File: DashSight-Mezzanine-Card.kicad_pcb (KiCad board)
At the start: 4 copper layers, 72 x 78.5 mm, 95 parts, among them IC2 ELM327, J1 Pi2 Connector, J10 QWIIC_CONNECTORJS-1MM, J14 1W-PC16, J15 1W-PC9, J2 Euler Connector, J3 Conn_Coaxial, J4 OBD2-DB9_Male, J5 Conn_02x05_Odd_Even, J6 Safeboot, J7 Reset, J8 QWIIC_CONNECTORJS-1MM, J9 QWIIC_CONNECTORJS-1MM, Q1 2N3904, Q2 2N3906, Q3 2N3906, Q4 2N3904, Q5 2N3904, Q6 2N3904, Q7 2N3904, SW1 SW_Push, SW2 SW_Push, U1 MCP2561-E/P, U2 LM317L_TO92, U3 LP2950-3.0_TO92, U4 ADuM1201AR, U5 NEO-M9N, U6 LSM9DS1, Y1 4.0MHz

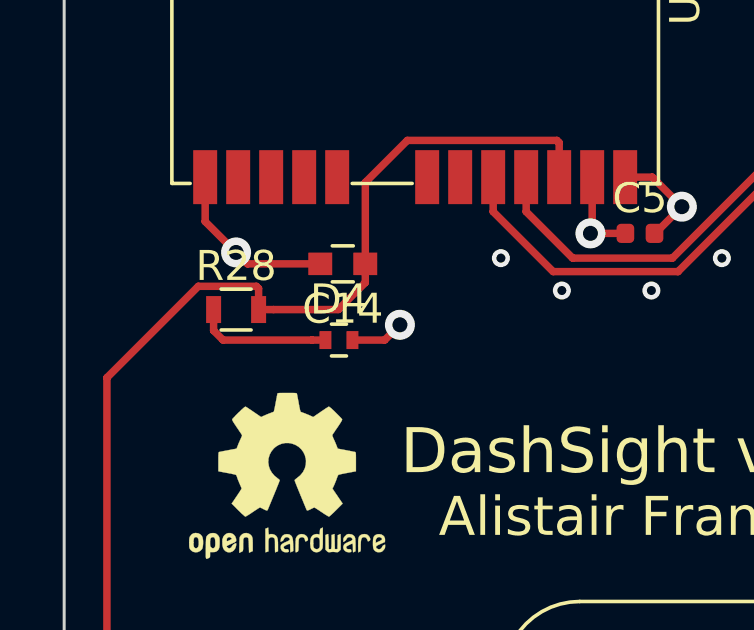
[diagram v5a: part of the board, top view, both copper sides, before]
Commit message: Update based on BOM avaliability
Signed-off-by: Alistair Francis <alistair@alistair23.me>
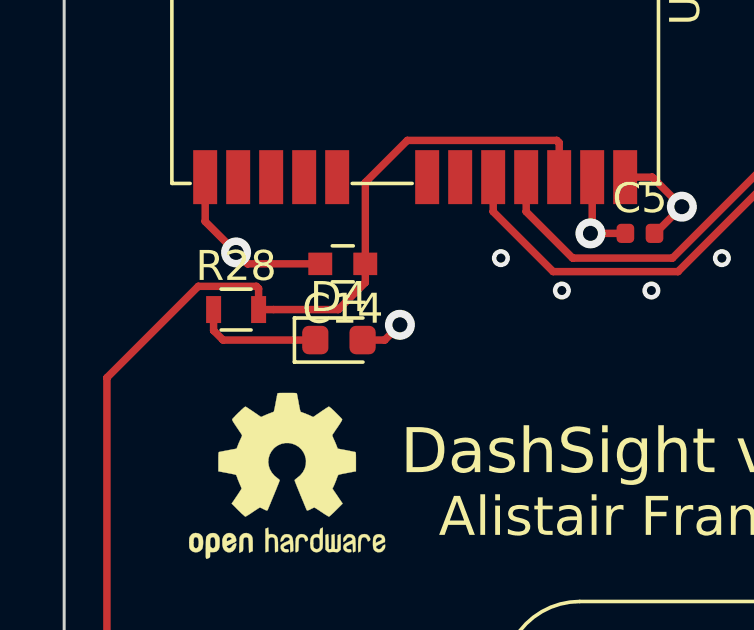
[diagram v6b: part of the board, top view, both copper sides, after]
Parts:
- D4: footprint Resistors_SMD:R_0402 -> Diode_SMD:D_0603_1608Metric
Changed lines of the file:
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@@
     (thickness 1.6)
     (drawings 6)
-    (tracks 916)
+    (tracks 915)
     (zones 0)
     (modules 95)
@@
     (uvia_drill 0.1)
   )
+  (module Diode_SMD:D_0603_1608Metric (layer F.Cu)
+    (at 137.16 76.2)
+    (descr "Diode SMD 0603 (1608 Metric), square (rectangular) end terminal, IPC_7351 nominal, (Body size source: http://www.tortai-tech.com/upload/download/2011102023233369053.pdf), generated with kicad-footprint-generator")
+    (tags diode)
+    (attr smd)
+    (fp_text reference D4 (at 0 -1.43) (layer F.SilkS)
+      (effects (font (size 1 1) (thickness 0.15)))
+    )
+    (fp_text value 0.5A/40V/420mV (at 0 1.43) (layer F.Fab)
+      (effects (font (size 1 1) (thickness 0.15)))
+    )
+    (fp_text user %R (at 0 0) (layer F.Fab)
+      (effects (font (size 0.4 0.4) (thickness 0.06)))
+    )
+    (fp_line (start 1.48 0.73) (end -1.48 0.73) (layer F.CrtYd) (width 0.05))
+    (fp_line (start 1.48 -0.73) (end 1.48 0.73) (layer F.CrtYd) (width 0.05))
+    (fp_line (start -1.48 -0.73) (end 1.48 -0.73) (layer F.CrtYd) (width 0.05))
+    (fp_line (start -1.48 0.73) (end -1.48 -0.73) (layer F.CrtYd) (width 0.05))
+    (fp_line (start -1.485 0.735) (end 0.8 0.735) (layer F.SilkS) (width 0.12))
+    (fp_line (start -1.485 -0.735) (end -1.485 0.735) (layer F.SilkS) (width 0.12))
+    (fp_line (start 0.8 -0.735) (end -1.485 -0.735) (layer F.SilkS) (width 0.12))
+    (fp_line (start 0.8 0.4) (end 0.8 -0.4) (layer F.Fab) (width 0.1))
+    (fp_line (start -0.8 0.4) (end 0.8 0.4) (layer F.Fab) (width 0.1))
+    (fp_line (start -0.8 -0.1) (end -0.8 0.4) (layer F.Fab) (width 0.1))
+    (fp_line (start -0.5 -0.4) (end -0.8 -0.1) (layer F.Fab) (width 0.1))
+    (fp_line (start 0.8 -0.4) (end -0.5 -0.4) (layer F.Fab) (width 0.1))
+    (pad 2 smd roundrect (at 0.7875 0) (size 0.875 0.95) (layers F.Cu F.Paste F.Mask) (roundrect_rratio 0.25)
+      (net 35 +3V3))
+    (pad 1 smd roundrect (at -0.7875 0) (size 0.875 0.95) (layers F.Cu F.Paste F.Mask) (roundrect_rratio 0.25)
+      (net 51 "Net-(D4-Pad1)"))
+    (model ${KISYS3DMOD}/Diode_SMD.3dshapes/D_0603_1608Metric.wrl
+      (at (xyz 0 0 0))
+      (scale (xyz 1 1 1))
+      (rotate (xyz 0 0 0))
+    )
+  )
   (module Crystal:Crystal_HC49-U_Vertical (layer F.Cu)
     (at 150.749 87.4395 180)
@@
     )
   )
-  (module Resistors_SMD:R_0402 (layer F.Cu)
-    (at 137.16 76.2)
-    (descr "Resistor SMD 0402, reflow soldering, Vishay (see dcrcw.pdf)")
-    (tags "resistor 0402")
-    (attr smd)
-    (fp_text reference D4 (at 0 -1.35) (layer F.SilkS)
-      (effects (font (size 1 1) (thickness 0.15)))
-    )
-    (fp_text value 0.5A/40V/420mV (at 0 1.45) (layer F.Fab)
-      (effects (font (size 1 1) (thickness 0.15)))
-    )
-    (fp_text user %R (at 0 -1.35) (layer F.Fab)
-      (effects (font (size 1 1) (thickness 0.15)))
-    )
-    (fp_line (start -0.5 0.25) (end -0.5 -0.25) (layer F.Fab) (width 0.1))
-    (fp_line (start 0.5 0.25) (end -0.5 0.25) (layer F.Fab) (width 0.1))
-    (fp_line (start 0.5 -0.25) (end 0.5 0.25) (layer F.Fab) (width 0.1))
-    (fp_line (start -0.5 -0.25) (end 0.5 -0.25) (layer F.Fab) (width 0.1))
-    (fp_line (start 0.25 -0.53) (end -0.25 -0.53) (layer F.SilkS) (width 0.12))
-    (fp_line (start -0.25 0.53) (end 0.25 0.53) (layer F.SilkS) (width 0.12))
-    (fp_line (start -0.8 -0.45) (end 0.8 -0.45) (layer F.CrtYd) (width 0.05))
-    (fp_line (start -0.8 -0.45) (end -0.8 0.45) (layer F.CrtYd) (width 0.05))
-    (fp_line (start 0.8 0.45) (end 0.8 -0.45) (layer F.CrtYd) (width 0.05))
-    (fp_line (start 0.8 0.45) (end -0.8 0.45) (layer F.CrtYd) (width 0.05))
-    (pad 1 smd rect (at -0.45 0) (size 0.4 0.6) (layers F.Cu F.Paste F.Mask)
-      (net 51 "Net-(D4-Pad1)"))
-    (pad 2 smd rect (at 0.45 0) (size 0.4 0.6) (layers F.Cu F.Paste F.Mask)
-      (net 35 +3V3))
-    (model ${KISYS3DMOD}/Resistors_SMD.3dshapes/R_0402.wrl
-      (at (xyz 0 0 0))
-      (scale (xyz 1 1 1))
-      (rotate (xyz 0 0 0))
-    )
-  )
   (module Diodes_SMD:D_SOD-123 (layer B.Cu)
     (at 146.939 115.824 180)
@@
   (gr_line (start 200 46.5) (end 200 125) (layer Edge.Cuts) (width 0.1))
   (gr_line (start 128 46.5) (end 200 46.5) (layer Edge.Cuts) (width 0.1))
+  (via (at 149.3139 53.2765) (size 0.6) (drill 0.3) (layers F.Cu B.Cu) (net 0))
   (via (at 138.4808 55.4228) (size 0.6) (drill 0.3) (layers F.Cu B.Cu) (net 1))
   (via (at 193.0908 59.7408) (size 0.8) (drill 0.4) (layers F.Cu B.Cu) (net 1))
@@
   (via (at 149.7203 58.0136) (size 0.6) (drill 0.3) (layers F.Cu B.Cu) (net 1))
   (via (at 149.7711 59.7789) (size 0.6) (drill 0.3) (layers F.Cu B.Cu) (net 1))
-  (via (at 149.3139 53.2765) (size 0.6) (drill 0.3) (layers F.Cu B.Cu) (net 0))
   (via (at 149.3139 54.4957) (size 0.6) (drill 0.3) (layers F.Cu B.Cu) (net 1))
   (via (at 151.0919 53.1241) (size 0.6) (drill 0.3) (layers F.Cu B.Cu) (net 1))
@@
   (segment (start 145.542 72.644) (end 146.708 72.644) (width 0.25) (layer F.Cu) (net 35))
   (segment (start 138.684 76.2) (end 139.192 75.692) (width 0.25) (layer F.Cu) (net 35))
-  (segment (start 137.61 76.2) (end 138.684 76.2) (width 0.25) (layer F.Cu) (net 35))
   (segment (start 187.706 121.963) (end 187.706 123.063) (width 0.25) (layer F.Cu) (net 35))
   (segment (start 187.781001 121.887999) (end 187.706 121.963) (width 0.25) (layer F.Cu) (net 35))
@@
   (segment (start 193.15684 74.76744) (end 192.9892 74.5998) (width 0.25) (layer F.Cu) (net 35))
   (segment (start 194.564 74.76744) (end 193.15684 74.76744) (width 0.25) (layer F.Cu) (net 35))
+  (segment (start 138.684 76.2) (end 137.9475 76.2) (width 0.25) (layer F.Cu) (net 35))
   (segment (start 141.0335 93.22963) (end 141.0335 94.361) (width 0.25) (layer F.Cu) (net 36))
   (segment (start 145.352999 86.364499) (end 141.0335 90.683998) (width 0.25) (layer F.Cu) (net 36))
@@
   (segment (start 164.792499 110.947501) (end 165.812501 110.947501) (width 0.25) (layer B.Cu) (net 50))
   (segment (start 157.7975 112.9665) (end 162.7735 112.9665) (width 0.25) (layer B.Cu) (net 50))
-  (segment (start 136.26 76.2) (end 136.71 76.2) (width 0.25) (layer F.Cu) (net 51))
-  (segment (start 133.297 76.2) (end 136.26 76.2) (width 0.25) (layer F.Cu) (net 51))
   (segment (start 132.981 75.884) (end 133.297 76.2) (width 0.25) (layer F.Cu) (net 51))
   (segment (start 132.981 75.184) (end 132.981 75.884) (width 0.25) (layer F.Cu) (net 51))
+  (segment (start 133.297 76.2) (end 136.3725 76.2) (width 0.25) (layer F.Cu) (net 51))
   (segment (start 140.3605 54.028) (end 140.081 54.3075) (width 0.25) (layer F.Cu) (net 52))
   (segment (start 140.3605 52.197) (end 140.3605 54.028) (width 0.25) (layer F.Cu) (net 52))
